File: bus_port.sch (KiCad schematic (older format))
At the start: 3 parts, among them P1 CONN_01X04, P1 CONN_01X40

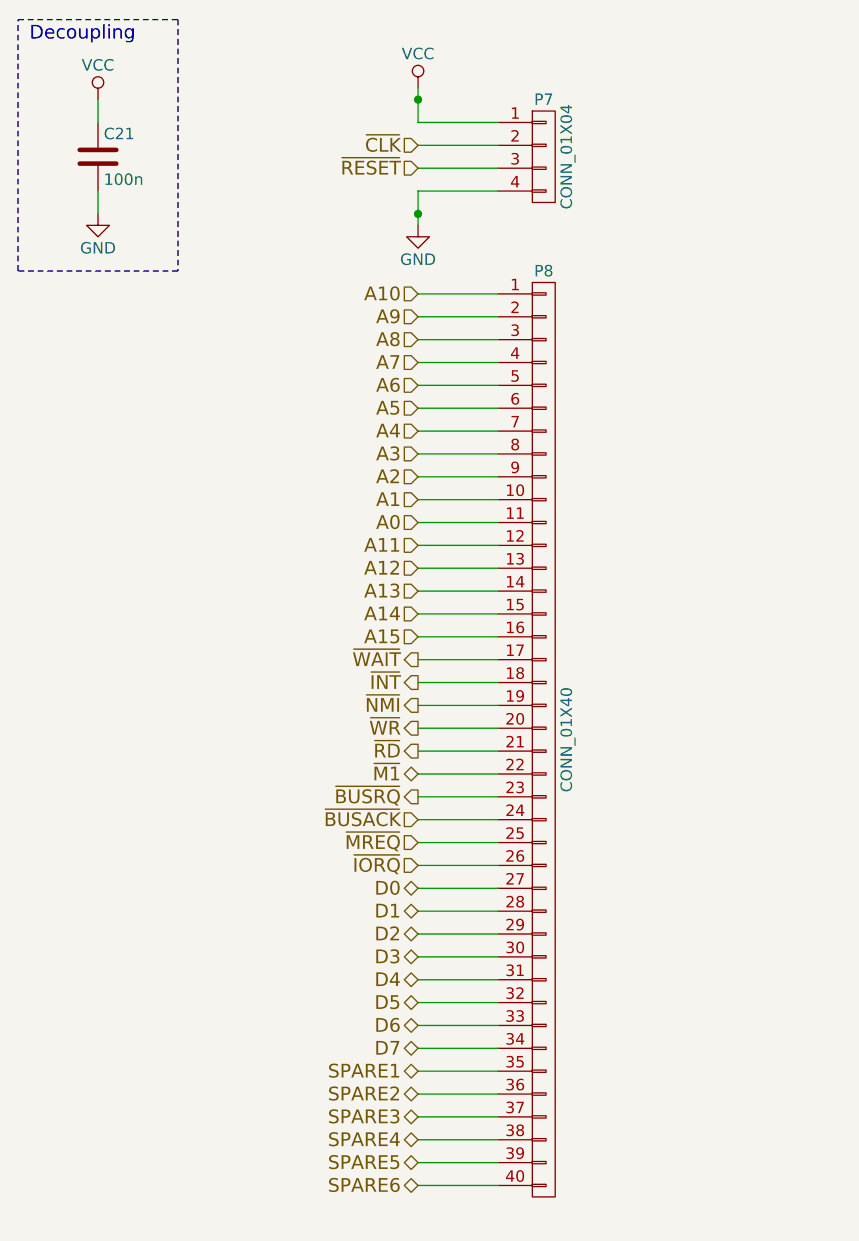
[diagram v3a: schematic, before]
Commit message: Update PCB, better layout. Got Addr bus back in order
Think having both USB and DC input would be useful. Switchmode a plus
then plugpack/battery etc voltage doesn't matter. Plus I have a bag full
of those parts too!

I've refdes'd the linear reg just to deal with the net. Will remove if
we both are happy with switcher. Linear cheaper to kit out I guess.

Was trying to find a better way to combine USB and DC power rails than
just schottky diodes. If you have any ideas.

Going to have a big area under the IO ports, might be worth adding a USB
to serial, or sacrifice a IO port for some blinky LEDs and buttons?
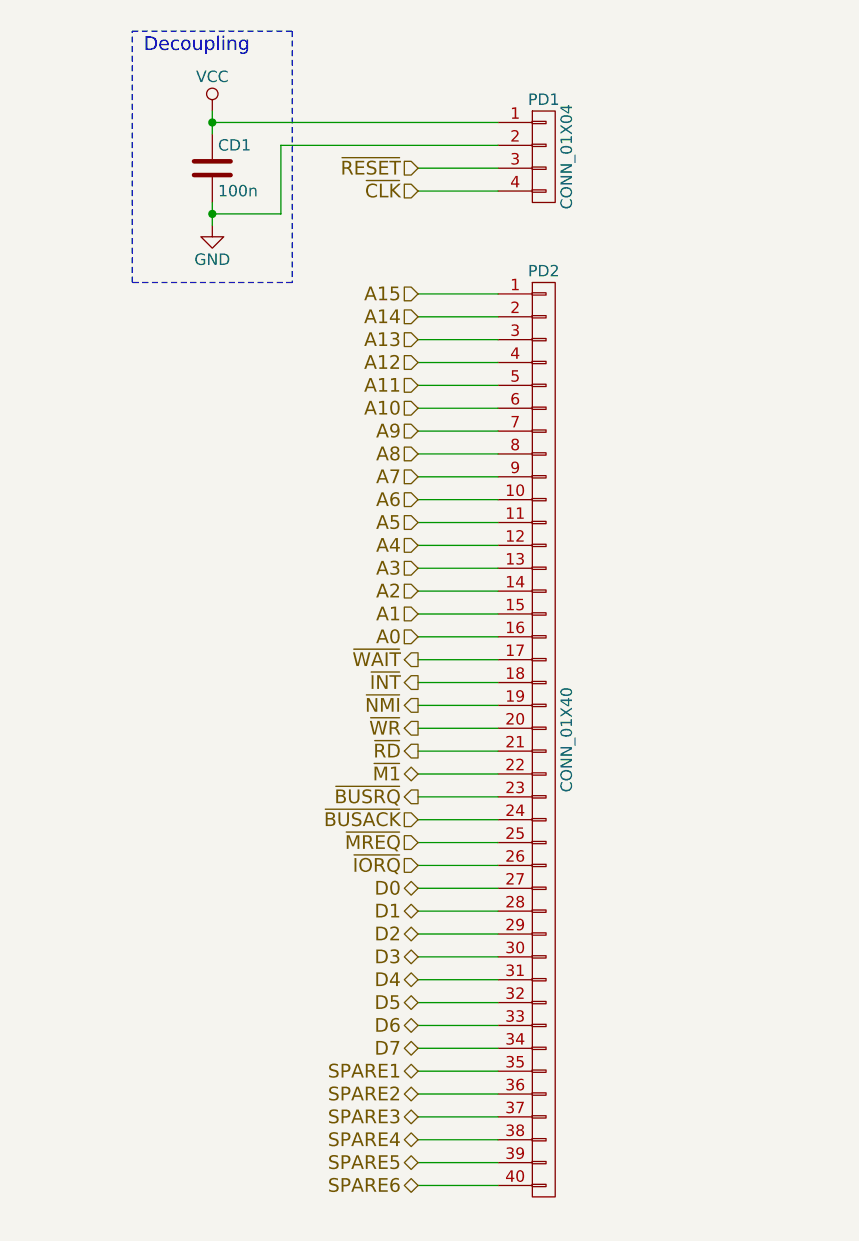
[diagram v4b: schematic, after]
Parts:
- PA1: renamed from P1; footprint Pin_Headers:Pin_Header_Straight_1x04 -> Socket_Strips:Socket_Strip_Straight_1x04
- renumbered C18 to CA1, P1 to PA2
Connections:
- net A0: now also PA2.16 (P16); no longer PA2.11 (P11)
- net A1: now also PA2.15 (P15); no longer PA2.10 (P10)
- net A10: now also PA2.6 (P6); no longer PA2.1 (P1)
- net A11: now also PA2.5 (P5); no longer PA2.12 (P12)
- net A12: now also PA2.4 (P4); no longer PA2.13 (P13)
- net A13: now also PA2.3 (P3); no longer PA2.14 (P14)
- net A14: now also PA2.2 (P2); no longer PA2.15 (P15)
- net A15: now also PA2.1 (P1); no longer PA2.16 (P16)
- net A2: now also PA2.14 (P14); no longer PA2.9 (P9)
- net A3: now also PA2.13 (P13); no longer PA2.8 (P8)
- net A4: now also PA2.12 (P12); no longer PA2.7 (P7)
- net A5: now also PA2.11 (P11); no longer PA2.6 (P6)
- net A6: now also PA2.10 (P10); no longer PA2.5 (P5)
- net A7: now also PA2.9 (P9); no longer PA2.4 (P4)
- net A8: now also PA2.8 (P8); no longer PA2.3 (P3)
- net A9: now also PA2.7 (P7); no longer PA2.2 (P2)
- net GND: now also PA1.2 (P2); no longer PA1.4 (P4)
- net ~CLK: now also PA1.4 (P4); no longer PA1.2 (P2)
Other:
- moved on the sheet: CD1
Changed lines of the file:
@@
 $Descr A4 11693 8268
 encoding utf-8
-Sheet 16 16
+Sheet 13 16
 Title ""
 Date ""
@@
 Comment4 ""
 $EndDescr
+Text HLabel 3900 4150 0    60   Input ~ 0
+A0
+Text HLabel 3900 4050 0    60   Input ~ 0
+A1
+Text HLabel 3900 3950 0    60   Input ~ 0
+A2
+Text HLabel 3900 3850 0    60   Input ~ 0
+A3
+Text HLabel 3900 3750 0    60   Input ~ 0
+A4
 Text HLabel 3900 3650 0    60   Input ~ 0
-A0
+A5
 Text HLabel 3900 3550 0    60   Input ~ 0
-A1
+A6
 Text HLabel 3900 3450 0    60   Input ~ 0
-A2
+A7
 Text HLabel 3900 3350 0    60   Input ~ 0
-A3
+A8
 Text HLabel 3900 3250 0    60   Input ~ 0
-A4
+A9
 Text HLabel 3900 3150 0    60   Input ~ 0
-A5
+A10
 Text HLabel 3900 3050 0    60   Input ~ 0
-A6
+A11
 Text HLabel 3900 2950 0    60   Input ~ 0
-A7
+A12
 Text HLabel 3900 2850 0    60   Input ~ 0
-A8
+A13
 Text HLabel 3900 2750 0    60   Input ~ 0
-A9
+A14
 Text HLabel 3900 2650 0    60   Input ~ 0
-A10
-Text HLabel 3900 3750 0    60   Input ~ 0
-A11
-Text HLabel 3900 3850 0    60   Input ~ 0
-A12
-Text HLabel 3900 3950 0    60   Input ~ 0
-A13
-Text HLabel 3900 4050 0    60   Input ~ 0
-A14
-Text HLabel 3900 4150 0    60   Input ~ 0
 A15
 Text HLabel 3900 5250 0    60   3State ~ 0
@@
 ~IORQ
 $Comp
-L CONN_01X40 P1
+L CONN_01X40 PA2
 U 1 1 577CEB68
 P 4450 4600
-AR Path="/577BB11C/577CEB68" Ref="P1"  Part="1"
-AR Path="/577C4BD1/577CEB68" Ref="P2"  Part="1"
-AR Path="/577F17CE/577F1897/577CEB68" Ref="P2"  Part="1"
-AR Path="/577F17CE/577F7EB3/577CEB68" Ref="P2"  Part="1"
-AR Path="/577F17CE/577F8AF5/577CEB68" Ref="P3"  Part="1"
-AR Path="/577F17CE/577F9440/577CEB68" Ref="P4"  Part="1"
-AR Path="/577F17CE/5782F6B6/577CEB68" Ref="P4"  Part="1"
-AR Path="/577F17CE/5783136E/577CEB68" Ref="P6"  Part="1"
-AR Path="/577F17CE/57832B70/577CEB68" Ref="P8"  Part="1"
-F 0 "P8" H 4450 6650 50  0000 C CNN
+AR Path="/577F17CE/577F1897/577CEB68" Ref="PA2"  Part="1"
+AR Path="/577F17CE/5782F6B6/577CEB68" Ref="PB2"  Part="1"
+AR Path="/577F17CE/5783136E/577CEB68" Ref="PC2"  Part="1"
+AR Path="/577F17CE/57832B70/577CEB68" Ref="PD2"  Part="1"
+F 0 "PD2" H 4450 6650 50  0000 C CNN
 F 1 "CONN_01X40" V 4550 4600 50  0000 C CNN
 F 2 "Socket_Strips:Socket_Strip_Straight_1x40" H 4450 4600 50  0001 C CNN
@@
 Wire Wire Line
 	3900 5150 4250 5150
-Text HLabel 3900 2000 0    60   Input ~ 0
+Text HLabel 3900 2200 0    60   Input ~ 0
 ~CLK
 $Comp
-L CONN_01X04 P1
+L CONN_01X04 PA1
 U 1 1 578144F7
 P 4450 2050
-AR Path="/577F17CE/577F1897/578144F7" Ref="P1"  Part="1"
-AR Path="/577F17CE/577F7EB3/578144F7" Ref="P6"  Part="1"
-AR Path="/577F17CE/577F8AF5/578144F7" Ref="P7"  Part="1"
-AR Path="/577F17CE/577F9440/578144F7" Ref="P8"  Part="1"
-AR Path="/577F17CE/5782F6B6/578144F7" Ref="P3"  Part="1"
-AR Path="/577F17CE/5783136E/578144F7" Ref="P5"  Part="1"
-AR Path="/577F17CE/57832B70/578144F7" Ref="P7"  Part="1"
-F 0 "P7" H 4450 2300 50  0000 C CNN
+AR Path="/577F17CE/577F1897/578144F7" Ref="PA1"  Part="1"
+AR Path="/577F17CE/5782F6B6/578144F7" Ref="PB1"  Part="1"
+AR Path="/577F17CE/5783136E/578144F7" Ref="PC1"  Part="1"
+AR Path="/577F17CE/57832B70/578144F7" Ref="PD1"  Part="1"
+F 0 "PD1" H 4450 2300 50  0000 C CNN
 F 1 "CONN_01X04" V 4550 2050 50  0000 C CNN
-F 2 "Pin_Headers:Pin_Header_Straight_1x04" H 4450 2050 50  0001 C CNN
+F 2 "Socket_Strips:Socket_Strip_Straight_1x04" H 4450 2050 50  0001 C CNN
 F 3 "" H 4450 2050 50  0000 C CNN
 	1    4450 2050
@@
 $EndComp
 Wire Wire Line
-	3900 1900 4250 1900
-Wire Wire Line
-	3900 1750 3900 1900
-$Comp
-L VCC #PWR046
-U 1 1 5781454A
-P 3900 1750
-AR Path="/577F17CE/577F1897/5781454A" Ref="#PWR046"  Part="1"
-AR Path="/577F17CE/577F7EB3/5781454A" Ref="#PWR019"  Part="1"
-AR Path="/577F17CE/577F8AF5/5781454A" Ref="#PWR021"  Part="1"
-AR Path="/577F17CE/577F9440/5781454A" Ref="#PWR023"  Part="1"
-AR Path="/577F17CE/5782F6B6/5781454A" Ref="#PWR050"  Part="1"
-AR Path="/577F17CE/5783136E/5781454A" Ref="#PWR054"  Part="1"
-AR Path="/577F17CE/57832B70/5781454A" Ref="#PWR058"  Part="1"
-F 0 "#PWR058" H 3900 1600 50  0001 C CNN
-F 1 "VCC" H 3900 1900 50  0000 C CNN
-F 2 "" H 3900 1750 50  0000 C CNN
-F 3 "" H 3900 1750 50  0000 C CNN
-	1    3900 1750
-	1    0    0    -1
-$EndComp
+	3000 1900 4250 1900
 Wire Wire Line
 	4250 2200 3900 2200
 Wire Wire Line
-	3900 2200 3900 2350
-$Comp
-L GND #PWR047
-U 1 1 5781458A
-P 3900 2350
-AR Path="/577F17CE/577F1897/5781458A" Ref="#PWR047"  Part="1"
-AR Path="/577F17CE/577F7EB3/5781458A" Ref="#PWR020"  Part="1"
-AR Path="/577F17CE/577F8AF5/5781458A" Ref="#PWR022"  Part="1"
-AR Path="/577F17CE/577F9440/5781458A" Ref="#PWR024"  Part="1"
-AR Path="/577F17CE/5782F6B6/5781458A" Ref="#PWR051"  Part="1"
-AR Path="/577F17CE/5783136E/5781458A" Ref="#PWR055"  Part="1"
-AR Path="/577F17CE/57832B70/5781458A" Ref="#PWR059"  Part="1"
-F 0 "#PWR059" H 3900 2100 50  0001 C CNN
-F 1 "GND" H 3900 2200 50  0000 C CNN
-F 2 "" H 3900 2350 50  0000 C CNN
-F 3 "" H 3900 2350 50  0000 C CNN
-	1    3900 2350
-	1    0    0    -1
-$EndComp
-Wire Wire Line
-	3900 2000 4250 2000
+	3300 2000 4250 2000
 Wire Wire Line
 	4250 2100 3900 2100
@@
 SPARE6
 $Comp
-L C C18
+L C CA1
 U 1 1 5780CE22
-P 2500 2050
-AR Path="/577F17CE/577F1897/5780CE22" Ref="C18"  Part="1"
-AR Path="/577F17CE/5782F6B6/5780CE22" Ref="C19"  Part="1"
-AR Path="/577F17CE/5783136E/5780CE22" Ref="C20"  Part="1"
-AR Path="/577F17CE/57832B70/5780CE22" Ref="C21"  Part="1"
-F 0 "C21" H 2525 2150 50  0000 L CNN
-F 1 "100n" H 2525 1950 50  0000 L CNN
-F 2 "Capacitors_SMD:C_0805_HandSoldering" H 2538 1900 50  0001 C CNN
-F 3 "" H 2500 2050 50  0000 C CNN
-	1    2500 2050
-	1    0    0    -1
-$EndComp
-Wire Wire Line
-	2500 1900 2500 1800
-Connection ~ 3900 1800
-Wire Wire Line
-	2500 2200 2500 2300
-Connection ~ 3900 2300
-$Comp
-L VCC #PWR048
+P 3000 2100
+AR Path="/577F17CE/577F1897/5780CE22" Ref="CA1"  Part="1"
+AR Path="/577F17CE/5782F6B6/5780CE22" Ref="CB2"  Part="1"
+AR Path="/577F17CE/5783136E/5780CE22" Ref="CC1"  Part="1"
+AR Path="/577F17CE/57832B70/5780CE22" Ref="CD1"  Part="1"
+F 0 "CD1" H 3025 2200 50  0000 L CNN
+F 1 "100n" H 3025 2000 50  0000 L CNN
+F 2 "Capacitors_SMD:C_0805_HandSoldering" H 3038 1950 50  0001 C CNN
+F 3 "" H 3000 2100 50  0000 C CNN
+	1    3000 2100
+	1    0    0    -1
+$EndComp
+Wire Wire Line
+	3000 1850 3000 1950
+Wire Wire Line
+	3000 2250 3000 2350
+$Comp
+L VCC #PWR057
 U 1 1 5780D6F2
-P 2500 1800
-AR Path="/577F17CE/577F1897/5780D6F2" Ref="#PWR048"  Part="1"
-AR Path="/577F17CE/5782F6B6/5780D6F2" Ref="#PWR052"  Part="1"
-AR Path="/577F17CE/5783136E/5780D6F2" Ref="#PWR056"  Part="1"
-AR Path="/577F17CE/57832B70/5780D6F2" Ref="#PWR060"  Part="1"
-F 0 "#PWR060" H 2500 1650 50  0001 C CNN
-F 1 "VCC" H 2500 1950 50  0000 C CNN
-F 2 "" H 2500 1800 50  0000 C CNN
-F 3 "" H 2500 1800 50  0000 C CNN
-	1    2500 1800
-	1    0    0    -1
-$EndComp
-$Comp
-L GND #PWR049
+P 3000 1850
+AR Path="/577F17CE/577F1897/5780D6F2" Ref="#PWR057"  Part="1"
+AR Path="/577F17CE/5782F6B6/5780D6F2" Ref="#PWR059"  Part="1"
+AR Path="/577F17CE/5783136E/5780D6F2" Ref="#PWR061"  Part="1"
+AR Path="/577F17CE/57832B70/5780D6F2" Ref="#PWR063"  Part="1"
+F 0 "#PWR063" H 3000 1700 50  0001 C CNN
+F 1 "VCC" H 3000 2000 50  0000 C CNN
+F 2 "" H 3000 1850 50  0000 C CNN
+F 3 "" H 3000 1850 50  0000 C CNN
+	1    3000 1850
+	1    0    0    -1
+$EndComp
+$Comp
+L GND #PWR058
 U 1 1 5780D706
-P 2500 2300
-AR Path="/577F17CE/577F1897/5780D706" Ref="#PWR049"  Part="1"
-AR Path="/577F17CE/5782F6B6/5780D706" Ref="#PWR053"  Part="1"
-AR Path="/577F17CE/5783136E/5780D706" Ref="#PWR057"  Part="1"
-AR Path="/577F17CE/57832B70/5780D706" Ref="#PWR061"  Part="1"
-F 0 "#PWR061" H 2500 2050 50  0001 C CNN
-F 1 "GND" H 2500 2150 50  0000 C CNN
-F 2 "" H 2500 2300 50  0000 C CNN
-F 3 "" H 2500 2300 50  0000 C CNN
-	1    2500 2300
-	1    0    0    -1
-$EndComp
-Text Notes 2200 1550 0    60   ~ 0
+P 3000 2350
+AR Path="/577F17CE/577F1897/5780D706" Ref="#PWR058"  Part="1"
+AR Path="/577F17CE/5782F6B6/5780D706" Ref="#PWR060"  Part="1"
+AR Path="/577F17CE/5783136E/5780D706" Ref="#PWR062"  Part="1"
+AR Path="/577F17CE/57832B70/5780D706" Ref="#PWR064"  Part="1"
+F 0 "#PWR064" H 3000 2100 50  0001 C CNN
+F 1 "GND" H 3000 2200 50  0000 C CNN
+F 2 "" H 3000 2350 50  0000 C CNN
+F 3 "" H 3000 2350 50  0000 C CNN
+	1    3000 2350
+	1    0    0    -1
+$EndComp
+Text Notes 2700 1600 0    60   ~ 0
 Decoupling
 Wire Notes Line
-	2150 1450 2850 1450
-Wire Notes Line
-	2850 1450 2850 2550
-Wire Notes Line
-	2850 2550 2150 2550
-Wire Notes Line
-	2150 2550 2150 1450
+	2650 1500 3350 1500
+Wire Notes Line
+	3350 1500 3350 2600
+Wire Notes Line
+	3350 2600 2650 2600
+Wire Notes Line
+	2650 2600 2650 1500
+Wire Wire Line
+	3300 2000 3300 2300
+Connection ~ 3000 1900
+Wire Wire Line
+	3300 2300 3000 2300
+Connection ~ 3000 2300
 $EndSCHEMATC

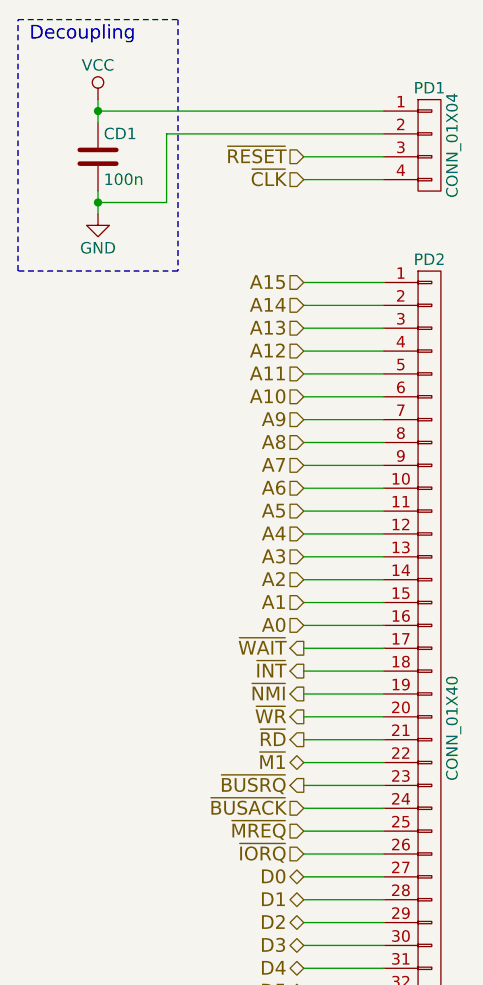
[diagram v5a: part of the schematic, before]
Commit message: Update with smaller board and through-hole parts.
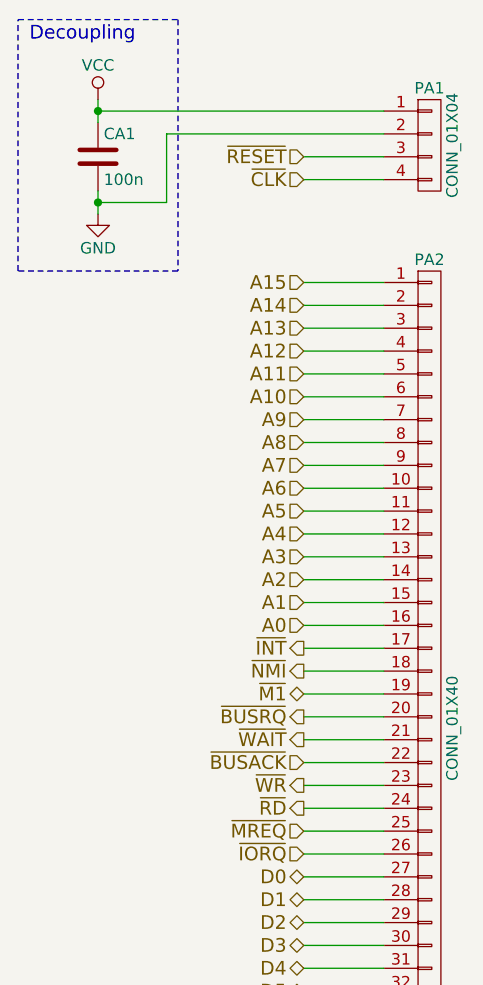
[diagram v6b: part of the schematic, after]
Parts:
- CA1: footprint Capacitors_SMD:C_0805_HandSoldering -> Capacitors_ThroughHole:C_Rect_L4_W2.5_P2.5
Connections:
- net ~BUSACK: now also PA2.22 (P22); no longer PA2.24 (P24)
- net ~BUSRQ: now also PA2.20 (P20); no longer PA2.23 (P23)
- net ~INT: now also PA2.17 (P17); no longer PA2.18 (P18)
- net ~M1: now also PA2.19 (P19); no longer PA2.22 (P22)
- net ~NMI: now also PA2.18 (P18); no longer PA2.19 (P19)
- net ~RD: now also PA2.24 (P24); no longer PA2.21 (P21)
- net ~WAIT: now also PA2.21 (P21); no longer PA2.17 (P17)
- net ~WR: now also PA2.23 (P23); no longer PA2.20 (P20)
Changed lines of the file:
@@
 $Descr A4 11693 8268
 encoding utf-8
-Sheet 13 16
+Sheet 9 11
 Title ""
 Date ""
@@
 Text HLabel 3900 5950 0    60   3State ~ 0
 D7
+Text HLabel 3900 4650 0    60   Output ~ 0
+~WAIT
 Text HLabel 3900 4250 0    60   Output ~ 0
-~WAIT
-Text HLabel 3900 4350 0    60   Output ~ 0
 ~INT
-Text HLabel 3900 4650 0    60   Output ~ 0
+Text HLabel 3900 4950 0    60   Output ~ 0
 ~RD
+Text HLabel 3900 4850 0    60   Output ~ 0
+~WR
+Text HLabel 3900 4450 0    60   3State ~ 0
+~M1
+Text HLabel 3900 4750 0    60   Input ~ 0
+~BUSACK
 Text HLabel 3900 4550 0    60   Output ~ 0
-~WR
-Text HLabel 3900 4750 0    60   3State ~ 0
-~M1
-Text HLabel 3900 4950 0    60   Input ~ 0
-~BUSACK
-Text HLabel 3900 4850 0    60   Output ~ 0
 ~BUSRQ
 Text HLabel 3900 5050 0    60   Input ~ 0
@@
 AR Path="/577F17CE/5783136E/577CEB68" Ref="PC2"  Part="1"
 AR Path="/577F17CE/57832B70/577CEB68" Ref="PD2"  Part="1"
-F 0 "PD2" H 4450 6650 50  0000 C CNN
+F 0 "PA2" H 4450 6650 50  0000 C CNN
 F 1 "CONN_01X40" V 4550 4600 50  0000 C CNN
 F 2 "Socket_Strips:Socket_Strip_Straight_1x40" H 4450 4600 50  0001 C CNN
@@
 AR Path="/577F17CE/5783136E/578144F7" Ref="PC1"  Part="1"
 AR Path="/577F17CE/57832B70/578144F7" Ref="PD1"  Part="1"
-F 0 "PD1" H 4450 2300 50  0000 C CNN
+F 0 "PA1" H 4450 2300 50  0000 C CNN
 F 1 "CONN_01X04" V 4550 2050 50  0000 C CNN
 F 2 "Socket_Strips:Socket_Strip_Straight_1x04" H 4450 2050 50  0001 C CNN
@@
 Wire Wire Line
 	4250 4450 3900 4450
-Text HLabel 3900 4450 0    60   Output ~ 0
+Text HLabel 3900 4350 0    60   Output ~ 0
 ~NMI
 Wire Wire Line
@@
 AR Path="/577F17CE/5783136E/5780CE22" Ref="CC1"  Part="1"
 AR Path="/577F17CE/57832B70/5780CE22" Ref="CD1"  Part="1"
-F 0 "CD1" H 3025 2200 50  0000 L CNN
+F 0 "CA1" H 3025 2200 50  0000 L CNN
 F 1 "100n" H 3025 2000 50  0000 L CNN
-F 2 "Capacitors_SMD:C_0805_HandSoldering" H 3038 1950 50  0001 C CNN
+F 2 "Capacitors_ThroughHole:C_Rect_L4_W2.5_P2.5" H 3038 1950 50  0001 C CNN
 F 3 "" H 3000 2100 50  0000 C CNN
 	1    3000 2100
@@
 	3000 2250 3000 2350
 $Comp
-L VCC #PWR051
+L VCC #PWR042
 U 1 1 5780D6F2
 P 3000 1850
-AR Path="/577F17CE/577F1897/5780D6F2" Ref="#PWR051"  Part="1"
-AR Path="/577F17CE/5782F6B6/5780D6F2" Ref="#PWR053"  Part="1"
-AR Path="/577F17CE/5783136E/5780D6F2" Ref="#PWR055"  Part="1"
+AR Path="/577F17CE/577F1897/5780D6F2" Ref="#PWR042"  Part="1"
+AR Path="/577F17CE/5782F6B6/5780D6F2" Ref="#PWR044"  Part="1"
+AR Path="/577F17CE/5783136E/5780D6F2" Ref="#PWR046"  Part="1"
 AR Path="/577F17CE/57832B70/5780D6F2" Ref="#PWR057"  Part="1"
-F 0 "#PWR057" H 3000 1700 50  0001 C CNN
+F 0 "#PWR042" H 3000 1700 50  0001 C CNN
 F 1 "VCC" H 3000 2000 50  0000 C CNN
 F 2 "" H 3000 1850 50  0000 C CNN
@@
 $EndComp
 $Comp
-L GND #PWR052
+L GND #PWR043
 U 1 1 5780D706
 P 3000 2350
-AR Path="/577F17CE/577F1897/5780D706" Ref="#PWR052"  Part="1"
-AR Path="/577F17CE/5782F6B6/5780D706" Ref="#PWR054"  Part="1"
-AR Path="/577F17CE/5783136E/5780D706" Ref="#PWR056"  Part="1"
+AR Path="/577F17CE/577F1897/5780D706" Ref="#PWR043"  Part="1"
+AR Path="/577F17CE/5782F6B6/5780D706" Ref="#PWR045"  Part="1"
+AR Path="/577F17CE/5783136E/5780D706" Ref="#PWR047"  Part="1"
 AR Path="/577F17CE/57832B70/5780D706" Ref="#PWR058"  Part="1"
-F 0 "#PWR058" H 3000 2100 50  0001 C CNN
+F 0 "#PWR043" H 3000 2100 50  0001 C CNN
 F 1 "GND" H 3000 2200 50  0000 C CNN
 F 2 "" H 3000 2350 50  0000 C CNN
